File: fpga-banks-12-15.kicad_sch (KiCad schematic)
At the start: 1 part, among them U8 XC7K160T-FFG676

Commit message: [#80386] Update Manufacturer of FPGA chip
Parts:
- U8: Manufacturer Xilinx -> AMD-Xilinx
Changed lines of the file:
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@@
 			)
 		)
-		(property "Description" ""
+		(property "Description" "FPGA Kintex-7 Family 162240 Cells 28nm Technology"
 			(at 59.055 90.805 0)
 			(effects
@@
 			)
 		)
-		(property "Manufacturer" "Xilinx"
+		(property "Manufacturer" "AMD-Xilinx"
 			(at 59.055 90.805 0)
 			(effects
@@
 			)
 		)
-		(property "Description" ""
+		(property "Description" "FPGA Kintex-7 Family 162240 Cells 28nm Technology"
 			(at 252.73 91.44 0)
 			(effects
@@
 			)
 		)
-		(property "Manufacturer" "Xilinx"
+		(property "Manufacturer" "AMD-Xilinx"
 			(at 252.73 91.44 0)
 			(effects
@@
 			)
 		)
-		(property "Description" ""
+		(property "Description" "FPGA Kintex-7 Family 162240 Cells 28nm Technology"
 			(at 325.12 91.44 0)
 			(effects
@@
 			)
 		)
-		(property "Manufacturer" "Xilinx"
+		(property "Manufacturer" "AMD-Xilinx"
 			(at 325.12 91.44 0)
 			(effects
@@
 			)
 		)
-		(property "Description" ""
+		(property "Description" "FPGA Kintex-7 Family 162240 Cells 28nm Technology"
 			(at 125.095 90.805 0)
 			(effects
@@
 			)
 		)
-		(property "Manufacturer" "Xilinx"
+		(property "Manufacturer" "AMD-Xilinx"
 			(at 125.095 90.805 0)
 			(effects

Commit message: [#80386] Add company name in board settings
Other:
- company: Antmicro Ltd. -> Antmicro
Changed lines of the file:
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@@
 		(date "2023-07-27")
 		(rev "1.0.1")
-		(company "Antmicro Ltd.")
+		(company "Antmicro")
 		(comment 1 "www.antmicro.com")
-		(comment 2 "Antmicro Ltd")
 	)
 	(text "BANK 13"

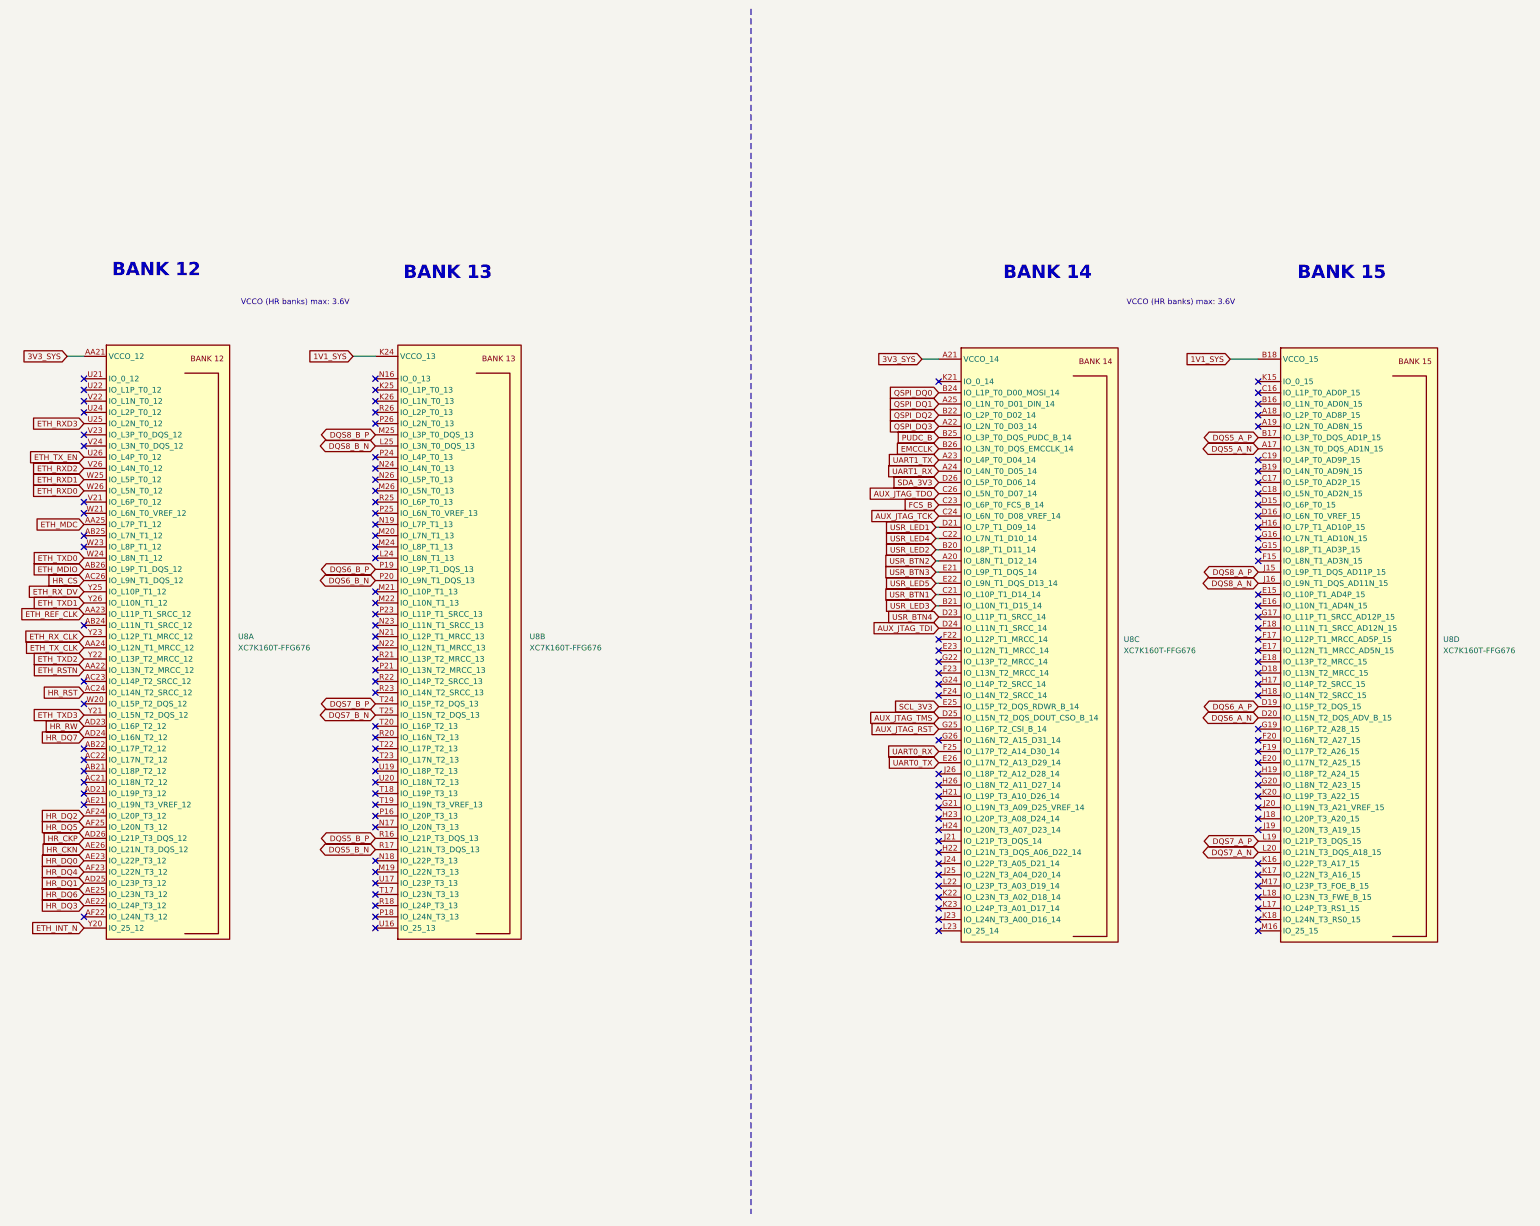
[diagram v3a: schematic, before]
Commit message: [#87036] Update components, clear DRC and ERC
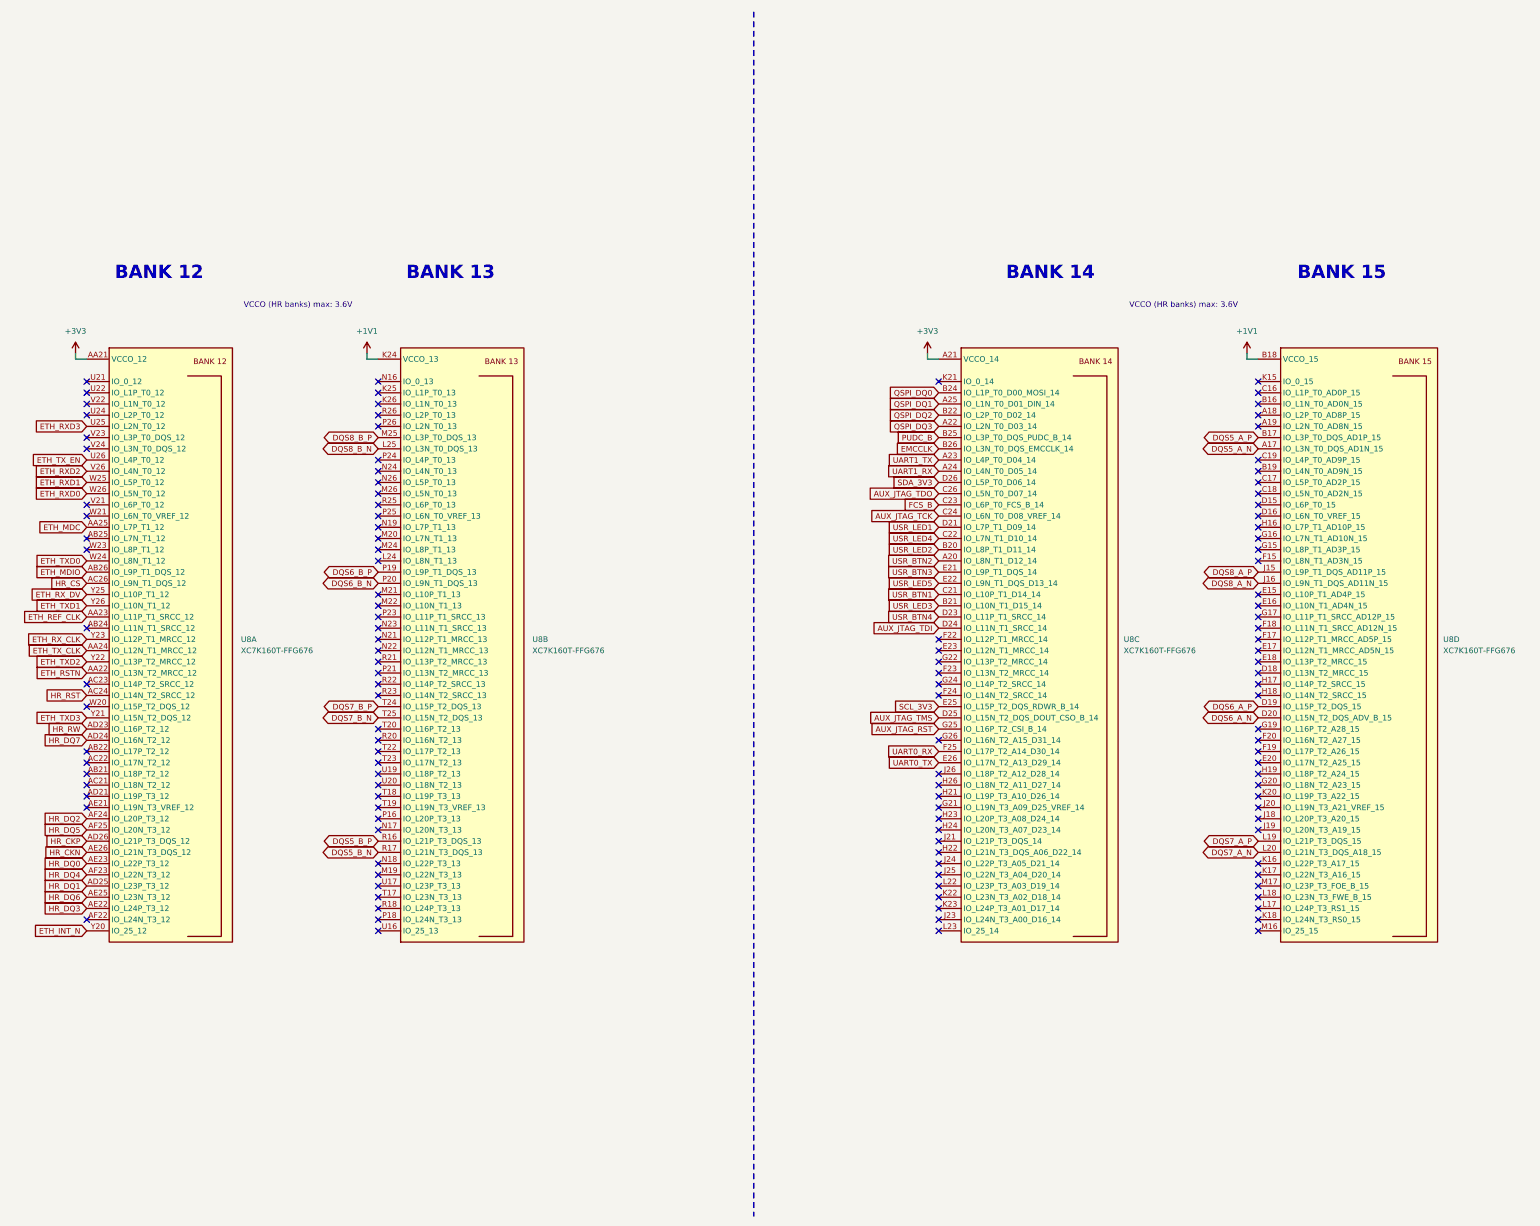
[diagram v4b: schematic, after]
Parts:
- U8: footprint data-center-rdimm-ddr5-tester-footprints:BGA-676_27x27mm_Layout26x26_P1X1mm -> antmicro-footprints:BGA-676_27x27mm_Layout26x26_P1x1mm_FFG676; symbol data-center-rdimm-ddr5-tester:XC7K160T-FFG676 -> antmicroFPGAChips:XC7K160T-FFG676
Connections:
- net 1V1_SYS renamed +1V1
- net 3V3_SYS renamed +3V3
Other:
- moved on the sheet: U8A, U8B
